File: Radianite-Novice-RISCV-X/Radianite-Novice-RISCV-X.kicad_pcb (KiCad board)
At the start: 2 copper layers, 68.6 x 53.3 mm, 145 parts, among them J1 USB_C_Receptacle_USB2.0_16P, J2 Conn_01x10_Pin, J3 Conn_01x08_Pin, J4 Conn_01x08, J5 Conn_01x06, J6 Barrel_Jack_Switch, J7 Radianite-Link, SW1 SW_Push, U1 CH32V305RBT6, U2 ESP32-C3-WROOM-02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

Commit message: fix some stuff ig
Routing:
- net /RESET: track 101.1 -> 103.4 mm
- net +3V3: track 183.6 -> 185.3 mm
- net /PROG_CLK: track 38.4 -> 37.4 mm
- net /D1: track 55.4 -> 54.6 mm
- net /RW5: track 102.3 -> 101.7 mm
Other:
- board text added: "D1"

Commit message: a lot of commit shit lol (PROJECT LEMON IRVINE FUCKED UP)
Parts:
- moved G*** 53.4 mm to (67.5, 57.2), turned to -90 degrees
- moved REF** 18.2 mm to (119.8, 71.2)
- moved G*** 1.25 mm to (111.3, 78.5)
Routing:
- net VBUS: track 110.6 -> 109.5 mm
- net /SCL: track 54.7 -> 54.0 mm
- net /PROG_CLK: track 37.4 -> 37.9 mm
- net GND: vias 46 -> 49
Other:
- board text added: "C"
- board text added: "REV 13/9/24 12:16 GMT+7 KICAD 8.0"
- board text added: "US"

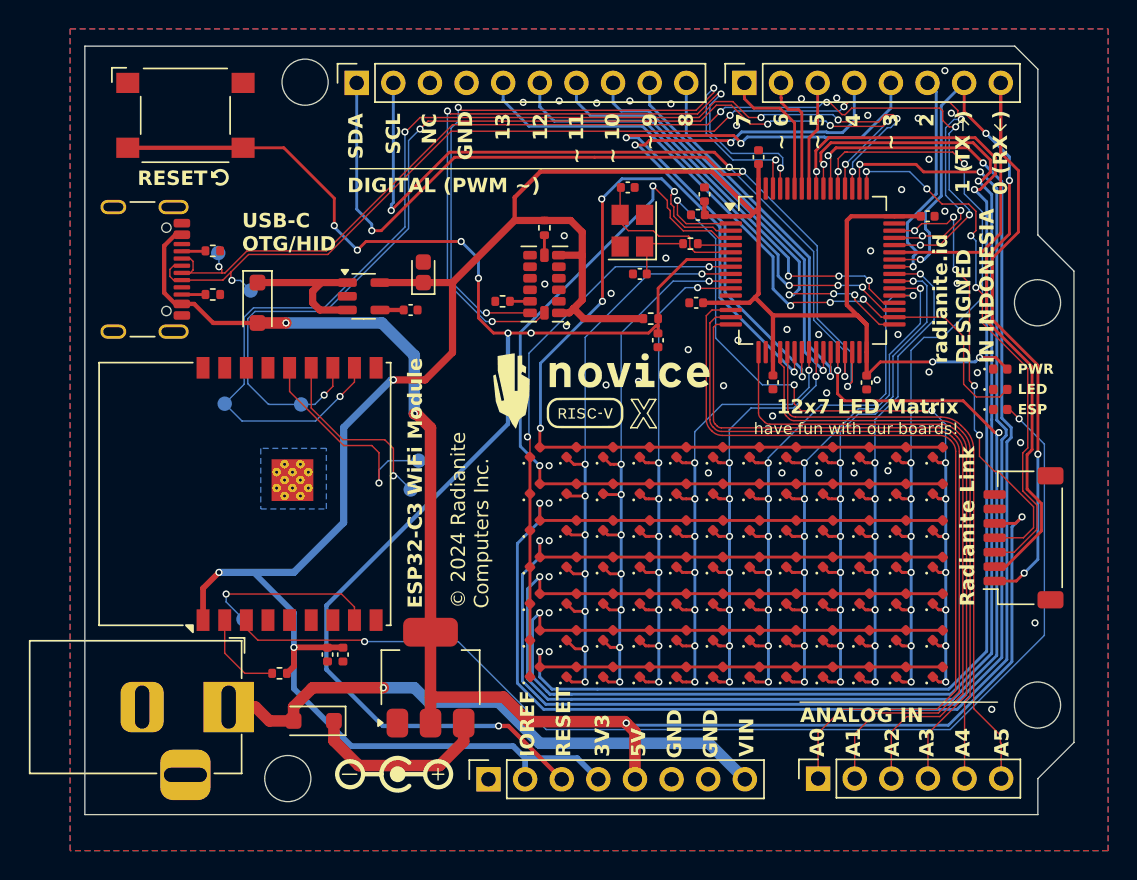
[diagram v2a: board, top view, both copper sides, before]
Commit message: fix some pcb (major rev, see on https://www.reddit.com/r/PrintedCircuitBoard/comments/1fpfia7/review_request_arduino_uno_r4_wifi_clone_using/)
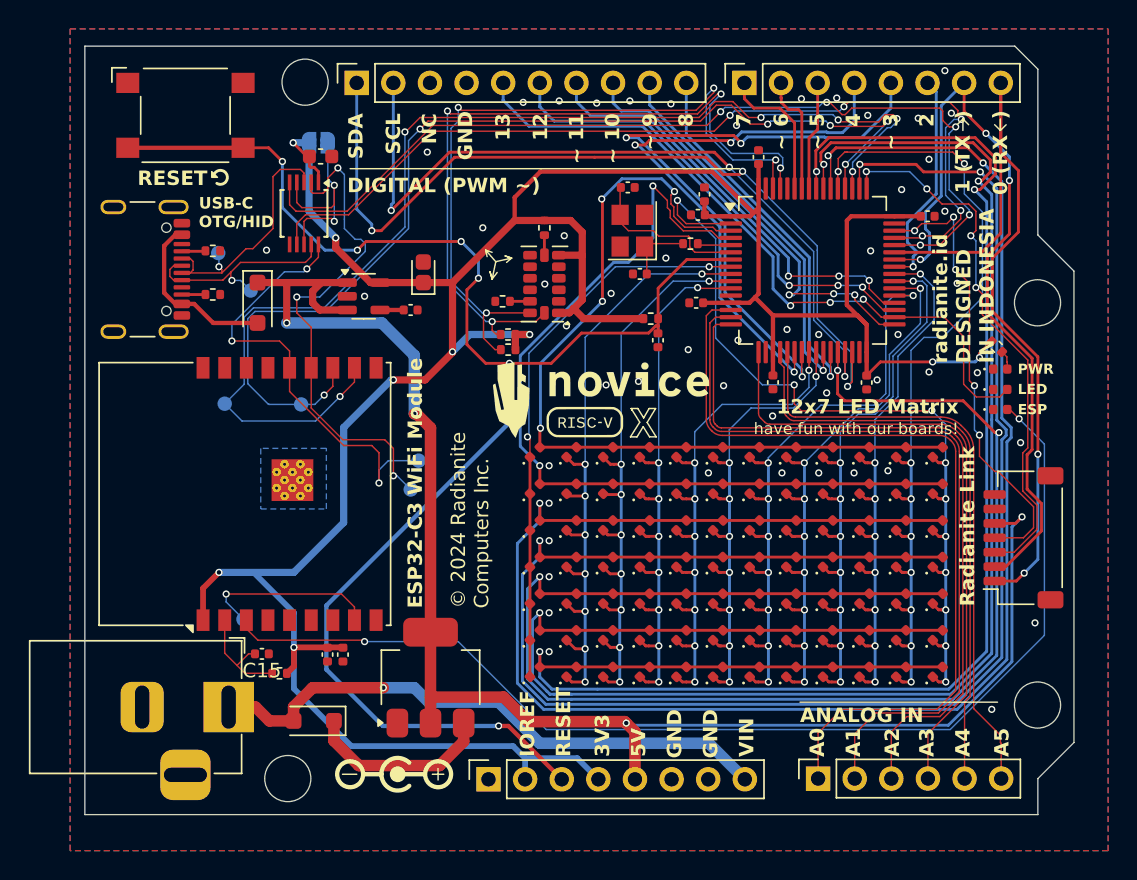
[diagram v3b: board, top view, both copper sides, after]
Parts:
- added C15: 1u, Capacitor_SMD:C_0402_1005Metric, F.Cu at (77.2, 75.2)
- added C16: 0.1u, Capacitor_SMD:C_0603_1608Metric, F.Cu at (81.2, 40.6)
- added JP1: SolderJumper_2_Open, Jumper:SolderJumper-2_P1.3mm_Open_RoundedPad1.0x1.5mm, B.Cu at (81.1, 39.7)
- added R10: 330, Resistor_SMD:R_0402_1005Metric, F.Cu at (128.2, 53.9)
- added R8: 1k, Resistor_SMD:R_0402_1005Metric, F.Cu at (94.3, 54.0)
- added R9: 1k, Resistor_SMD:R_0402_1005Metric, F.Cu at (94.2, 53.0)
- added U6: TS3A24159DGS, Package_SO:TSSOP-10_3x3mm_P0.5mm, F.Cu at (80.1, 44.6)
- moved REF** 1.25 mm to (121.0, 71.2)
- moved G*** 0.63 mm to (100.7, 57.5)
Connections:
- D2 pad 1: Net-(D2-K) -> VBUS
- D2 pad 2: VBUS -> Net-(D2-A)
- D3 pad 2: +3V3 -> Net-(D3-A)
- J1 pad A4: VBUS -> Net-(D2-A)
- J1 pad A9: VBUS -> Net-(D2-A)
- J1 pad B4: VBUS -> Net-(D2-A)
- J1 pad B9: VBUS -> Net-(D2-A)
- U1 pad 44: /USB_DM -> /RV_DM
- U1 pad 45: /USB_DP -> /RV_DP
- U4 pad 1: Net-(D2-K) -> VBUS
- U4 pad 3: Net-(D2-K) -> VBUS
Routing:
- net /RV_DM: track 0.00 -> 65.5 mm, vias 0 -> 5
- net /RV_DP: track 0.00 -> 65.0 mm, vias 0 -> 5
- net /USB_DP: track 77.7 -> 15.1 mm, vias 6 -> 1
- net /USB_DM: track 76.8 -> 18.1 mm, vias 6 -> 1
- net +3V3: track 185.3 -> 209.4 mm, vias 5 -> 9
- net /ESP_DM: track 13.1 -> 35.0 mm, vias 1 -> 3
- net /ESP_DP: track 15.6 -> 31.1 mm, vias 1 -> 3
- net Net-(JP1-A): track 0.00 -> 15.1 mm, vias 0 -> 2
- net Net-(D2-A): track 0.00 -> 12.1 mm
- net Net-(D2-K): track 10.5 -> 0.00 mm
- net /GYRO_SDA: track 48.4 -> 51.7 mm
- net /RESET: track 103.4 -> 106.0 mm, vias 7 -> 6
- net Net-(U2-EN): track 6.16 -> 7.74 mm
- net Net-(D3-A): track 0.00 -> 1.34 mm
- net /GYRO_SCL: track 50.6 -> 51.9 mm
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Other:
- board text added: "Bridge: ESP32 USB HID/PROG"
- board text added: "Open: CH32 USB HID/PROG"
- board text added: "Programming modes"
- board text added: "REV 26/9/24 20:03 GMT+7 KICAD 8.0"
- board text added: "RX>TX"
- board text added: "TX > RX"
- board text added: "unleash.the.maker.in.you."
- board text removed: "REV 13/9/24 12:16 GMT+7 KICAD 8.0"
- board text removed: "RX"
- board text removed: "TX"
- board text removed: "open and cheap computing and hardware engineering for everyone of all ages."

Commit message: fix some stuff violating clearances and adding current limiting resistor
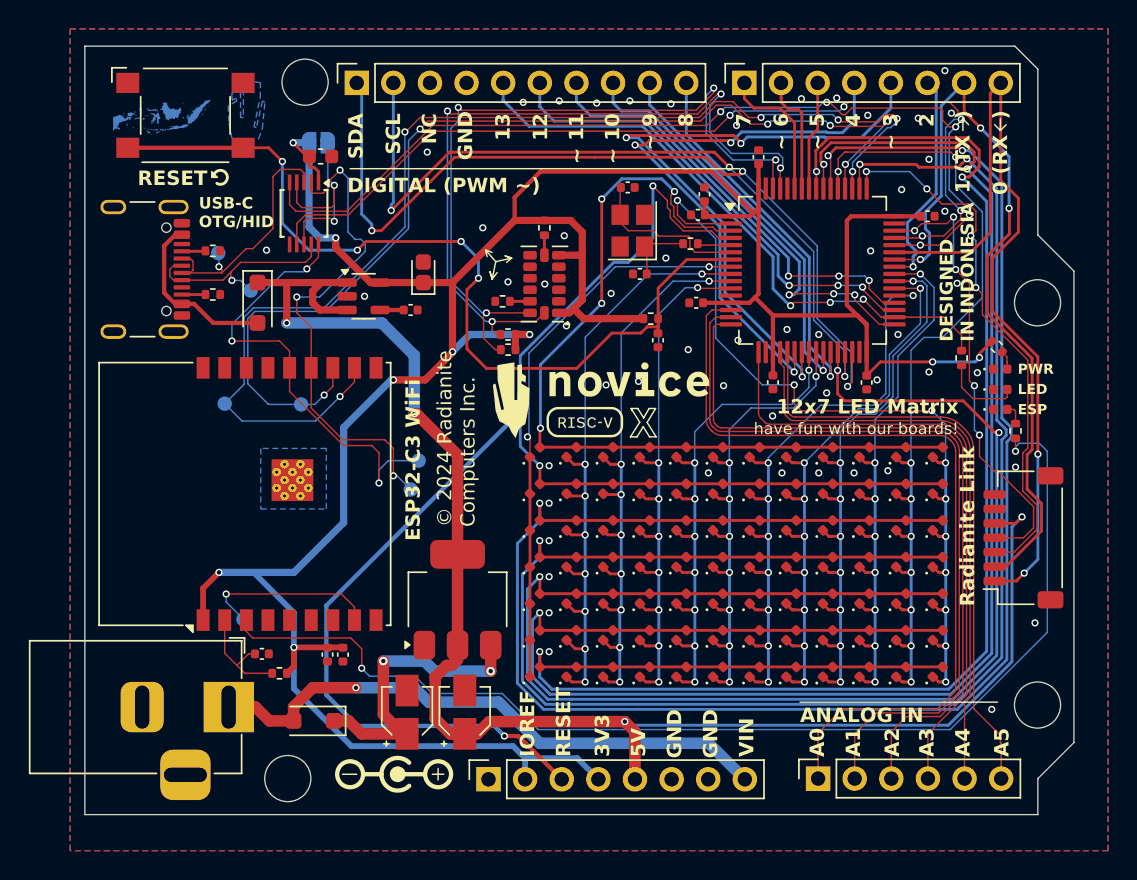
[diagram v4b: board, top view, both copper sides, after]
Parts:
- added C17: 47u, Capacitor_SMD:CP_Elec_3x5.3, F.Cu at (87.2, 79.2)
- added C18: 47u, Capacitor_SMD:CP_Elec_3x5.3, F.Cu at (91.2, 79.2)
- added G***: LOGO, LOGO, B.Cu at (70.2, 37.9)
- added R11: 330, Resistor_SMD:R_0402_1005Metric, F.Cu at (125.7, 54.6)
- added R12: 330, Resistor_SMD:R_0402_1005Metric, F.Cu at (129.4, 59.7)
- moved U3 5.72 mm to (90.8, 71.4)
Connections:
- D4 pad 2: /D13 -> Net-(D4-A)
- U2 pad 3: Net-(D5-A) -> Net-(U2-IO4)
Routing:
- net Net-(U2-IO4): track 0.00 -> 79.0 mm, vias 0 -> 2
- net Net-(D5-A): track 78.4 -> 1.50 mm, vias 2 -> 0
- net Net-(D1-K): track 13.1 -> 20.9 mm, vias 0 -> 2
- net /D13: track 48.5 -> 42.6 mm
- net Net-(D4-A): track 0.00 -> 5.58 mm
- net /RESET: track 106.0 -> 107.8 mm
- net VBUS: track 108.6 -> 109.9 mm
- net /RW6: track 117.5 -> 116.8 mm
- net +3V3: track 209.4 -> 210.0 mm
- net /RW7: track 114.6 -> 114.1 mm
- net GND: vias 53 -> 54
- added copper zone on B.Cu, net (none)
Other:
- board text added: "DESIGNED IN INDONESIA"
- board text added: "ESP32-C3 WiFi"
- board text added: "REV 27/9/24 18:44 GMT+7 KICAD 8.0"
- board text removed: "ESP32-C3 WiFi Module"
- board text removed: "REV 26/9/24 20:03 GMT+7 KICAD 8.0"
- board text removed: "radianite.id DESIGNED IN INDONESIA"

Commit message: my bad for using nightly kicad
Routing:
- net Net-(JP1-A): track 15.1 -> 13.0 mm
- net /RV_DM: track 65.5 -> 64.3 mm, vias 5 -> 4
- net /RV_DP: track 65.0 -> 65.5 mm, vias 5 -> 4
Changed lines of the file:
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@@
 		)
 		(fp_text user "${REFERENCE}"
-			(at 0 0 360)
+			(at 0 0 0)
 			(layer "F.Fab")
 			(effects
@@
 	)
 	(segment
-		(start 123.85 37.3)
-		(end 118.086397 37.3)
+		(start 79.1 42.953554)
+		(end 79.896446 43.75)
 		(width 0.1)
 		(layer "F.Cu")
@@
 	)
 	(segment
-		(start 122.85 46.8)
-		(end 124.189951 46.8)
+		(start 79.1 42.45)
+		(end 79.1 42.953554)
 		(width 0.1)
 		(layer "F.Cu")
@@
 	)
 	(segment
-		(start 79.1 42.45)
-		(end 79.1 44)
+		(start 83.786397 43.75)
+		(end 89.036397 38.5)
 		(width 0.1)
 		(layer "F.Cu")
@@
 	)
 	(segment
-		(start 83.086397 44.45)
-		(end 89.036397 38.5)
+		(start 123.85 37.3)
+		(end 118.086397 37.3)
+		(width 0.1)
+		(layer "F.Cu")
+		(net 91)
+	)
+	(segment
+		(start 122.85 46.8)
+		(end 124.189951 46.8)
 		(width 0.1)
 		(layer "F.Cu")
@@
 	)
 	(segment
-		(start 108.044744 38.5)
-		(end 108.997372 37.547372)
+		(start 124.4 38.15)
+		(end 124.4 37.5)
 		(width 0.1)
 		(layer "F.Cu")
@@
 	)
 	(segment
-		(start 124.4 38.15)
-		(end 124.4 37.5)
+		(start 125.3 38.6)
+		(end 124.85 38.6)
 		(width 0.1)
 		(layer "F.Cu")
@@
 	)
 	(segment
-		(start 79.1 44)
-		(end 79.55 44.45)
+		(start 117.408888 37.741111)
+		(end 116.567777 36.9)
 		(width 0.1)
 		(layer "F.Cu")
@@
 	)
 	(segment
-		(start 125.3 38.6)
-		(end 124.85 38.6)
+		(start 79.896446 43.75)
+		(end 83.786397 43.75)
 		(width 0.1)
 		(layer "F.Cu")
@@
 	)
 	(segment
-		(start 117.408888 37.741111)
-		(end 116.567777 36.9)
+		(start 117.636397 37.75)
+		(end 117.6 37.75)
 		(width 0.1)
 		(layer "F.Cu")
@@
 	)
 	(segment
-		(start 117.636397 37.75)
-		(end 117.6 37.75)
+		(start 108.044744 38.5)
+		(end 108.997372 37.547372)
 		(width 0.1)
 		(layer "F.Cu")
@@
 	)
 	(segment
-		(start 79.55 44.45)
-		(end 83.086397 44.45)
-		(width 0.1)
-		(layer "F.Cu")
-		(net 91)
-	)
-	(segment
 		(start 124.189951 46.8)
 		(end 126.25 44.739951)
@@
 	)
 	(via
-		(at 122.85 46.8)
-		(size 0.5)
-		(drill 0.3)
-		(layers "F.Cu" "B.Cu")
-		(net 91)
-	)
-	(via
 		(at 116.35 36.9)
 		(size 0.5)
@@
 	)
 	(segment
-		(start 122.852786 46.3)
-		(end 122.987974 46.164812)
+		(start 83.889951 44)
+		(end 79.9 44)
 		(width 0.1)
 		(layer "F.Cu")
@@
 	)
 	(segment
-		(start 88.989951 38.9)
-		(end 83.189951 44.7)
-		(width 0.1)
-		(layer "F.Cu")
-		(net 92)
-	)
-	(segment
-		(start 124.886397 36.9)
-		(end 117.85 36.9)
+		(start 124.336397 46.3)
+		(end 125.65 44.986397)
 		(width 0.1)
 		(layer "F.Cu")
@@
 	)
 	(segment
-		(start 108.55 38.9)
-		(end 88.989951 38.9)
+		(start 88.989951 38.9)
+		(end 83.889951 44)
 		(width 0.1)
 		(layer "F.Cu")
@@
 	)
 	(segment
-		(start 124.471585 46.164812)
-		(end 125.65 44.986397)
+		(start 124.886397 36.9)
+		(end 117.85 36.9)
 		(width 0.1)
 		(layer "F.Cu")
@@
 	)
 	(segment
-		(start 80.2 44.7)
-		(end 79.6 45.3)
+		(start 79.6 44.3)
+		(end 79.6 46.75)
 		(width 0.1)
 		(layer "F.Cu")
@@
 	)
 	(segment
-		(start 122.987974 46.164812)
-		(end 124.471585 46.164812)
-		(width 0.1)
-		(layer "F.Cu")
-		(net 92)
-	)
-	(segment
 		(start 125.45 37.463603)
 		(end 124.886397 36.9)
@@
 	)
 	(segment
-		(start 83.189951 44.7)
-		(end 80.2 44.7)
+		(start 108.55 38.9)
+		(end 88.989951 38.9)
 		(width 0.1)
 		(layer "F.Cu")
@@
 	)
 	(segment
-		(start 79.6 45.3)
-		(end 79.6 46.75)
+		(start 121.05 46.3)
+		(end 124.336397 46.3)
 		(width 0.1)
 		(layer "F.Cu")
@@
 	)
 	(segment
-		(start 125.45 37.839996)
-		(end 125.45 37.463603)
+		(start 79.9 44)
+		(end 79.6 44.3)
 		(width 0.1)
 		(layer "F.Cu")
@@
 	)
 	(segment
-		(start 121.05 46.3)
-		(end 122.852786 46.3)
+		(start 125.45 37.839996)
+		(end 125.45 37.463603)
 		(width 0.1)
 		(layer "F.Cu")
@@
 	)
 	(via
-		(at 122.987974 46.164812)
-		(size 0.5)
-		(drill 0.3)
-		(layers "F.Cu" "B.Cu")
-		(net 92)
-	)
-	(via
 		(at 125.690002 38.079998)
 		(size 0.5)
@@
 	)
 	(segment
-		(start 82.2 42.65)
-		(end 82.2 44)
-		(width 0.1)
-		(layer "F.Cu")
-		(net 93)
-	)
-	(segment
-		(start 80.1 45.153554)
-		(end 80.303554 44.95)
+		(start 79.6 43.1)
+		(end 79.6 42.45)
 		(width 0.1)
 		(layer "F.Cu")
@@
 	)
 	(segment
-		(start 82.2 44)
-		(end 82 44.2)
+		(start 80 43.5)
+		(end 79.6 43.1)
 		(width 0.1)
 		(layer "F.Cu")
@@
 	)
 	(segment
-		(start 82 44.2)
-		(end 79.95 44.2)
+		(start 82.2 42.65)
+		(end 82.2 42.8)
 		(width 0.1)
 		(layer "F.Cu")
@@
 	)
 	(segment
-		(start 80.1 46.75)
-		(end 80.1 45.153554)
+		(start 81.5 43.5)
+		(end 80 43.5)
 		(width 0.1)
 		(layer "F.Cu")
@@
 	)
 	(segment
-		(start 80.303554 44.95)
-		(end 82 44.95)
+		(start 82.2 44.9)
+		(end 80.353554 44.9)
 		(width 0.1)
 		(layer "F.Cu")
@@
 	)
 	(segment
-		(start 79.95 44.2)
-		(end 79.6 43.85)
+		(start 82.2 42.8)
+		(end 81.5 43.5)
 		(width 0.1)
 		(layer "F.Cu")
@@
 	)
 	(segment
-		(start 82 44.95)
-		(end 82.2 45.15)
+		(start 80.353554 44.9)
+		(end 80.1 45.153554)
 		(width 0.1)
 		(layer "F.Cu")
@@
 	)
 	(segment
-		(start 79.6 43.85)
-		(end 79.6 42.45)
+		(start 80.1 45.153554)
+		(end 80.1 46.75)
 		(width 0.1)
 		(layer "F.Cu")
@@
 	)
 	(via
-		(at 82.2 45.15)
+		(at 82.2 44.9)
 		(size 0.5)
 		(drill 0.3)
@@
 	)
 	(segment
-		(start 82.2 45.15)
+		(start 82.2 44.9)
 		(end 82.2 42.65)
 		(width 0.1)

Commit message: revisi
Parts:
- removed the G*** at (100.7, 57.5)
- removed the G*** at (100.6, 46.2)
- added G***: LOGO, LOGO, F.Cu at (102.6, 57.6)
- added G***: LOGO, LOGO, B.Cu at (105.5, 46.1)
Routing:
- net +3V3: track 210.0 -> 209.4 mm
- net GND: vias 54 -> 67
- net /PROG_DIO: vias 5 -> 4
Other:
- board text added: "REV 18/10/24 10:57 GMT+7 KICAD 8.0"
- board text added: "unleash.the.maker.in.you"
- board text removed: "REV 27/9/24 18:44 GMT+7 KICAD 8.0"
- board text removed: "unleash.the.maker.in.you."
